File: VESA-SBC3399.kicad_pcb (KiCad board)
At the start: 2 copper layers, 54 parts, among them U1 RK3399

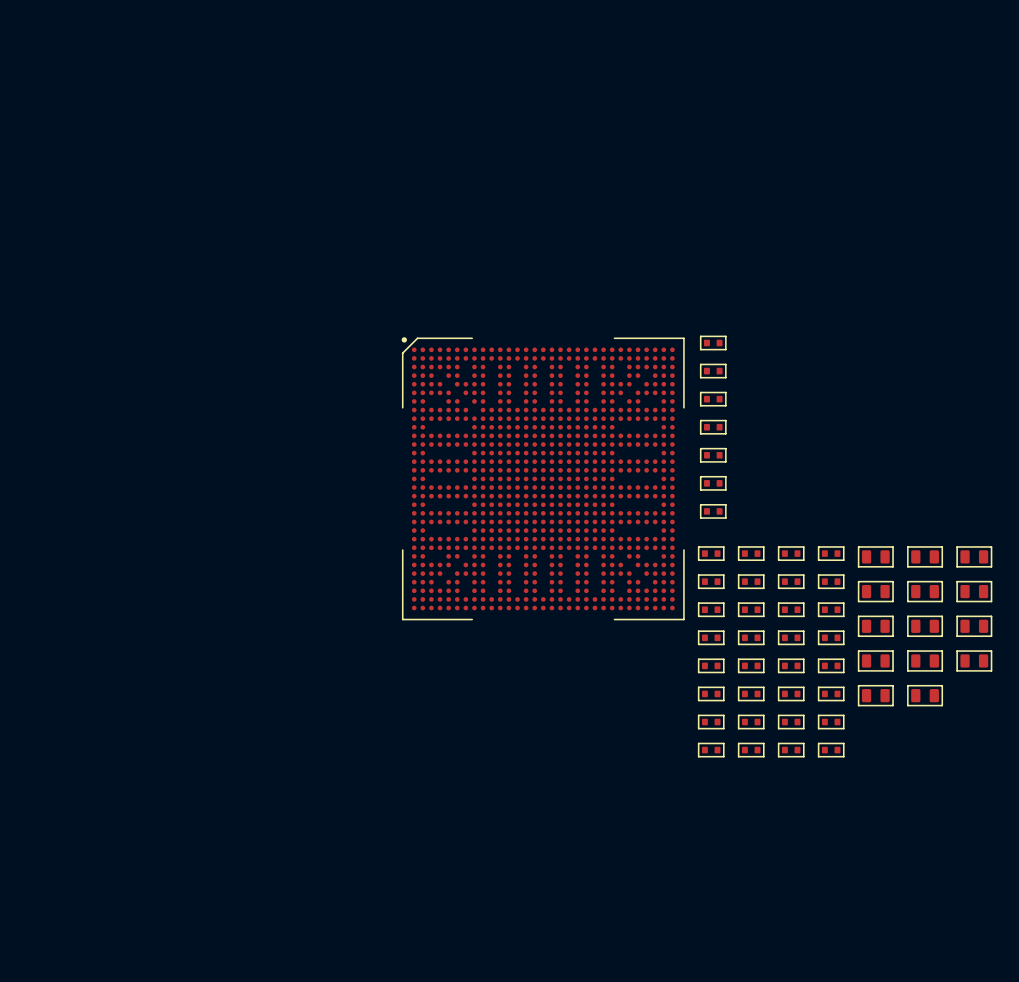
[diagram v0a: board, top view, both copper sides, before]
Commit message: design USB-A
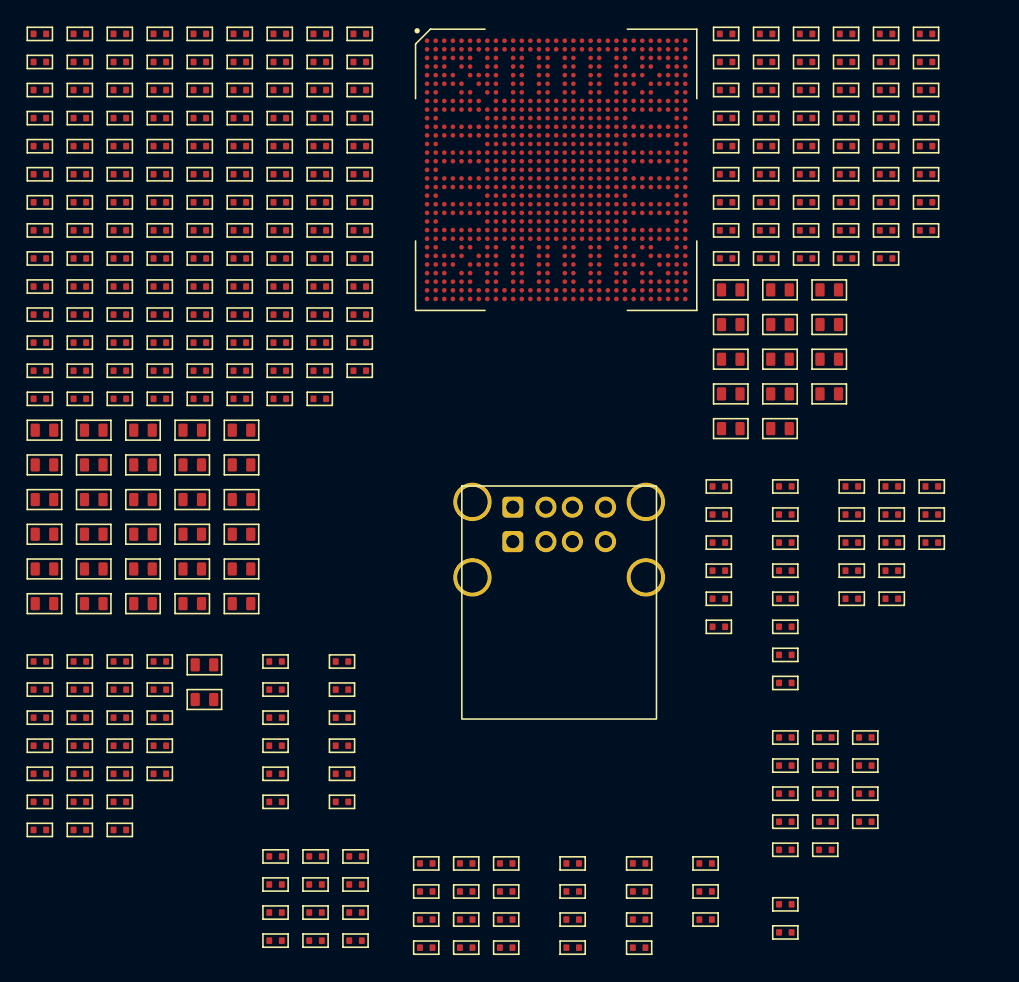
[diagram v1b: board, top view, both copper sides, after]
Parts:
- removed C1, C11, C12, C25, C26, C27, C48, C5, C6: ~, footprints:CAPC1005X50N
- removed C22, C3, C35, C36: ~, footprints:CAPC1608X80N
- removed U1: RK3399, footprints:BGA828C65P31X31_2100X2100X161
- added C100: ~, footprints:CAPC1005X50N, F.Cu at (125.8, 64.6)
- added C101: ~, footprints:CAPC1005X50N, F.Cu at (125.8, 66.8)
- added C102: ~, footprints:CAPC1005X50N, F.Cu at (125.8, 68.9)
- added C103: ~, footprints:CAPC1608X80N, F.Cu at (129.0, 97.2)
- added C104: ~, footprints:CAPC1005X50N, F.Cu at (125.8, 71.0)
- added C105: ~, footprints:CAPC1005X50N, F.Cu at (125.8, 73.1)
- added C106: ~, footprints:CAPC1005X50N, F.Cu at (125.8, 75.2)
- added C107: ~, footprints:CAPC1005X50N, F.Cu at (125.8, 77.4)
- added C108: ~, footprints:CAPC1005X50N, F.Cu at (125.8, 79.5)
- added C109: ~, footprints:CAPC1005X50N, F.Cu at (125.8, 81.6)
- added C110: ~, footprints:CAPC1005X50N, F.Cu at (125.8, 83.7)
- added C111: ~, footprints:CAPC1005X50N, F.Cu at (125.8, 85.8)
- added C112: ~, footprints:CAPC1608X80N, F.Cu at (129.0, 99.8)
- added C113: ~, footprints:CAPC1005X50N, F.Cu at (125.8, 88.0)
- added C114: ~, footprints:CAPC1005X50N, F.Cu at (125.8, 90.1)
- added C115: ~, footprints:CAPC1005X50N, F.Cu at (125.8, 92.2)
- added C116: ~, footprints:CAPC1005X50N, F.Cu at (128.8, 64.6)
- added C117: ~, footprints:CAPC1005X50N, F.Cu at (128.8, 66.8)
- added C118: ~, footprints:CAPC1005X50N, F.Cu at (128.8, 68.9)
- added C119: ~, footprints:CAPC1005X50N, F.Cu at (128.8, 71.0)
- added C120: ~, footprints:CAPC1608X80N, F.Cu at (129.0, 102.4)
- added C121: ~, footprints:CAPC1608X80N, F.Cu at (129.0, 105.0)
- added C122: ~, footprints:CAPC1005X50N, F.Cu at (128.8, 73.1)
- added C123: ~, footprints:CAPC1005X50N, F.Cu at (128.8, 75.2)
- added C124: ~, footprints:CAPC1005X50N, F.Cu at (128.8, 77.4)
- added C125: ~, footprints:CAPC1608X80N, F.Cu at (129.0, 107.7)
- added C126: ~, footprints:CAPC1005X50N, F.Cu at (128.8, 79.5)
- added C127: ~, footprints:CAPC1005X50N, F.Cu at (128.8, 81.6)
- added C128: ~, footprints:CAPC1005X50N, F.Cu at (128.8, 83.7)
- added C129: ~, footprints:CAPC1005X50N, F.Cu at (128.8, 85.8)
- added C130: ~, footprints:CAPC1005X50N, F.Cu at (128.8, 88.0)
- added C131: ~, footprints:CAPC1005X50N, F.Cu at (128.8, 90.1)
- added C132: ~, footprints:CAPC1005X50N, F.Cu at (165.6, 64.6)
- added C133: ~, footprints:CAPC1608X80N, F.Cu at (165.9, 84.0)
- added C134: ~, footprints:CAPC1608X80N, F.Cu at (165.9, 86.6)
- added C135: ~, footprints:CAPC1608X80N, F.Cu at (165.9, 89.2)
- added C136: ~, footprints:CAPC1005X50N, F.Cu at (165.6, 66.8)
- added C137: ~, footprints:CAPC1005X50N, F.Cu at (165.6, 68.9)
- added C138: ~, footprints:CAPC1005X50N, F.Cu at (165.6, 71.0)
- added C139: ~, footprints:CAPC1005X50N, F.Cu at (165.6, 73.1)
- added C140: ~, footprints:CAPC1005X50N, F.Cu at (165.6, 75.2)
- added C141: ~, footprints:CAPC1005X50N, F.Cu at (165.6, 77.4)
- added C142: ~, footprints:CAPC1005X50N, F.Cu at (165.6, 79.5)
- added C143: ~, footprints:CAPC1005X50N, F.Cu at (165.6, 81.6)
- added C144: ~, footprints:CAPC1608X80N, F.Cu at (165.9, 91.8)
- added C145: ~, footprints:CAPC1608X80N, F.Cu at (165.9, 94.5)
- added C146: ~, footprints:CAPC1005X50N, F.Cu at (168.6, 64.6)
- added C147: ~, footprints:CAPC1005X50N, F.Cu at (168.6, 66.8)
- added C148: ~, footprints:CAPC1005X50N, F.Cu at (168.6, 68.9)
- added C149: ~, footprints:CAPC1005X50N, F.Cu at (168.6, 71.0)
- added C150: ~, footprints:CAPC1005X50N, F.Cu at (168.6, 73.1)
- added C151: ~, footprints:CAPC1005X50N, F.Cu at (168.6, 75.2)
- added C152: ~, footprints:CAPC1005X50N, F.Cu at (168.6, 77.4)
- added C153: ~, footprints:CAPC1608X80N, F.Cu at (169.6, 84.0)
- added C154: ~, footprints:CAPC1608X80N, F.Cu at (169.6, 86.6)
- added C155: ~, footprints:CAPC1608X80N, F.Cu at (169.6, 89.2)
- added C156: ~, footprints:CAPC1005X50N, F.Cu at (168.6, 79.5)
- added C157: ~, footprints:CAPC1005X50N, F.Cu at (168.6, 81.6)
- added C158: ~, footprints:CAPC1005X50N, F.Cu at (171.6, 64.6)
- added C159: ~, footprints:CAPC1005X50N, F.Cu at (171.6, 66.8)
- added C160: ~, footprints:CAPC1005X50N, F.Cu at (171.6, 68.9)
- added C161: ~, footprints:CAPC1005X50N, F.Cu at (171.6, 71.0)
- added C162: ~, footprints:CAPC1005X50N, F.Cu at (171.6, 73.1)
- added C163: ~, footprints:CAPC1005X50N, F.Cu at (171.6, 75.2)
- added C164: ~, footprints:CAPC1608X80N, F.Cu at (169.6, 91.8)
- added C165: ~, footprints:CAPC1608X80N, F.Cu at (169.6, 94.5)
- added C166: ~, footprints:CAPC1608X80N, F.Cu at (173.3, 84.0)
- added C167: ~, footprints:CAPC1608X80N, F.Cu at (173.3, 86.6)
- added C168: ~, footprints:CAPC1005X50N, F.Cu at (171.6, 77.4)
- added C169: ~, footprints:CAPC1608X80N, F.Cu at (173.3, 89.2)
- added C170: ~, footprints:CAPC1005X50N, F.Cu at (171.6, 79.5)
- added C171: ~, footprints:CAPC1005X50N, F.Cu at (171.6, 81.6)
- added C172: ~, footprints:CAPC1005X50N, F.Cu at (174.6, 64.6)
- added C173: ~, footprints:CAPC1005X50N, F.Cu at (174.6, 66.8)
- added C174: ~, footprints:CAPC1005X50N, F.Cu at (174.6, 68.9)
- added C175: ~, footprints:CAPC1005X50N, F.Cu at (174.6, 71.0)
- added C176: ~, footprints:CAPC1005X50N, F.Cu at (174.6, 73.1)
- added C177: ~, footprints:CAPC1608X80N, F.Cu at (173.3, 91.8)
- added C178: ~, footprints:CAPC1005X50N, F.Cu at (174.6, 75.2)
- added C179: ~, footprints:CAPC1005X50N, F.Cu at (174.6, 77.4)
- added C180: ~, footprints:CAPC1005X50N, F.Cu at (174.6, 79.5)
- added C181: ~, footprints:CAPC1005X50N, F.Cu at (174.6, 81.6)
- added C182: ~, footprints:CAPC1005X50N, F.Cu at (177.6, 64.6)
- added C183: ~, footprints:CAPC1005X50N, F.Cu at (177.6, 66.8)
- added C184: ~, footprints:CAPC1005X50N, F.Cu at (177.6, 68.9)
- added C185: ~, footprints:CAPC1005X50N, F.Cu at (177.6, 71.0)
- added C186: ~, footprints:CAPC1005X50N, F.Cu at (177.6, 73.1)
- added C187: ~, footprints:CAPC1005X50N, F.Cu at (177.6, 75.2)
- added C188: ~, footprints:CAPC1005X50N, F.Cu at (177.6, 77.4)
- added C189: ~, footprints:CAPC1005X50N, F.Cu at (177.6, 79.5)
- added C190: ~, footprints:CAPC1005X50N, F.Cu at (177.6, 81.6)
- added C191: ~, footprints:CAPC1005X50N, F.Cu at (180.7, 64.6)
- added C192: ~, footprints:CAPC1005X50N, F.Cu at (180.7, 66.8)
- added C193: ~, footprints:CAPC1005X50N, F.Cu at (180.7, 68.9)
- added C194: ~, footprints:CAPC1005X50N, F.Cu at (180.7, 71.0)
- added C195: ~, footprints:CAPC1005X50N, F.Cu at (180.7, 73.1)
- added C196: ~, footprints:CAPC1005X50N, F.Cu at (180.7, 75.2)
- added C197: ~, footprints:CAPC1005X50N, F.Cu at (142.9, 127.3)
- added C198: ~, footprints:CAPC1005X50N, F.Cu at (142.9, 129.4)
- added C199: ~, footprints:CAPC1005X50N, F.Cu at (142.9, 131.5)
- added C200: ~, footprints:CAPC1005X50N, F.Cu at (142.9, 133.7)
- added C201: ~, footprints:CAPC1005X50N, F.Cu at (145.9, 127.3)
- added C202: ~, footprints:CAPC1005X50N, F.Cu at (159.0, 127.3)
- added C203: ~, footprints:CAPC1005X50N, F.Cu at (159.0, 129.4)
- added C204: ~, footprints:CAPC1005X50N, F.Cu at (170.0, 130.4)
- added C205: ~, footprints:CAPC1005X50N, F.Cu at (170.0, 132.5)
- added C206: ~, footprints:CAPC1005X50N, F.Cu at (170.0, 98.8)
- added C207: ~, footprints:CAPC1005X50N, F.Cu at (170.0, 100.9)
- added C208: ~, footprints:CAPC1608X80N, F.Cu at (126.2, 112.3)
- added C209: ~, footprints:CAPC1005X50N, F.Cu at (113.7, 112.0)
- added C210: ~, footprints:CAPC1005X50N, F.Cu at (113.7, 114.2)
- added C211: ~, footprints:CAPC1005X50N, F.Cu at (113.7, 116.3)
- added C212: ~, footprints:CAPC1005X50N, F.Cu at (113.7, 118.4)
- added C213: ~, footprints:CAPC1005X50N, F.Cu at (113.7, 120.5)
- added C214: ~, footprints:CAPC1005X50N, F.Cu at (113.7, 122.6)
- added C215: ~, footprints:CAPC1005X50N, F.Cu at (113.7, 124.8)
- added C216: ~, footprints:CAPC1005X50N, F.Cu at (116.7, 112.0)
- added C217: ~, footprints:CAPC1608X80N, F.Cu at (126.2, 114.9)
- added C218: ~, footprints:CAPC1005X50N, F.Cu at (116.7, 114.2)
- added C219: ~, footprints:CAPC1005X50N, F.Cu at (116.7, 116.3)
- added C220: ~, footprints:CAPC1005X50N, F.Cu at (116.7, 118.4)
- added C221: ~, footprints:CAPC1005X50N, F.Cu at (116.7, 120.5)
- added C222: ~, footprints:CAPC1005X50N, F.Cu at (116.7, 122.6)
- added C223: ~, footprints:CAPC1005X50N, F.Cu at (116.7, 124.8)
- added C224: ~, footprints:CAPC1005X50N, F.Cu at (119.8, 112.0)
- added C225: ~, footprints:CAPC1005X50N, F.Cu at (119.8, 114.2)
- added C226: ~, footprints:CAPC1005X50N, F.Cu at (119.8, 116.3)
- added C227: ~, footprints:CAPC1005X50N, F.Cu at (119.8, 118.4)
- added C228: ~, footprints:CAPC1005X50N, F.Cu at (119.8, 120.5)
- added C229: ~, footprints:CAPC1005X50N, F.Cu at (119.8, 122.6)
- added C230: ~, footprints:CAPC1005X50N, F.Cu at (119.8, 124.8)
- added C231: ~, footprints:CAPC1005X50N, F.Cu at (122.8, 112.0)
- added C232: ~, footprints:CAPC1005X50N, F.Cu at (175.0, 98.8)
- added C233: ~, footprints:CAPC1005X50N, F.Cu at (175.0, 100.9)
- added C234: ~, footprints:CAPC1005X50N, F.Cu at (175.0, 103.1)
- added C235: ~, footprints:CAPC1005X50N, F.Cu at (175.0, 105.2)
- added C236: ~, footprints:CAPC1005X50N, F.Cu at (175.0, 107.3)
- added C237: ~, footprints:CAPC1005X50N, F.Cu at (178.1, 98.8)
- added C238: ~, footprints:CAPC1005X50N, F.Cu at (178.1, 100.9)
- added C239: ~, footprints:CAPC1005X50N, F.Cu at (178.1, 103.1)
- added C240: ~, footprints:CAPC1005X50N, F.Cu at (178.1, 105.2)
- added C241: ~, footprints:CAPC1005X50N, F.Cu at (154.0, 127.3)
- added C242: ~, footprints:CAPC1005X50N, F.Cu at (154.0, 129.4)
- added C243: ~, footprints:CAPC1005X50N, F.Cu at (164.0, 127.3)
- added C244: ~, footprints:CAPC1005X50N, F.Cu at (170.0, 117.8)
- added C245: ~, footprints:CAPC1005X50N, F.Cu at (170.0, 119.9)
- added C246: ~, footprints:CAPC1005X50N, F.Cu at (170.0, 122.0)
- added C247: ~, footprints:CAPC1005X50N, F.Cu at (170.0, 124.1)
- added C248: ~, footprints:CAPC1005X50N, F.Cu at (131.5, 126.8)
- added C54: ~, footprints:CAPC1005X50N, F.Cu at (116.7, 92.2)
- added C56: ~, footprints:CAPC1005X50N, F.Cu at (119.8, 64.6)
- added C57: ~, footprints:CAPC1005X50N, F.Cu at (119.8, 66.8)
- added C58: ~, footprints:CAPC1005X50N, F.Cu at (119.8, 68.9)
- added C59: ~, footprints:CAPC1608X80N, F.Cu at (117.8, 107.7)
- added C60: ~, footprints:CAPC1608X80N, F.Cu at (121.5, 94.6)
- added C61: ~, footprints:CAPC1005X50N, F.Cu at (119.8, 71.0)
- added C62: ~, footprints:CAPC1005X50N, F.Cu at (119.8, 73.1)
- added C63: ~, footprints:CAPC1005X50N, F.Cu at (119.8, 75.2)
- added C64: ~, footprints:CAPC1608X80N, F.Cu at (121.5, 97.2)
- added C65: ~, footprints:CAPC1608X80N, F.Cu at (121.5, 99.8)
- added C66: ~, footprints:CAPC1608X80N, F.Cu at (121.5, 102.4)
- added C67: ~, footprints:CAPC1005X50N, F.Cu at (119.8, 77.4)
- added C68: ~, footprints:CAPC1005X50N, F.Cu at (119.8, 79.5)
- added C69: ~, footprints:CAPC1005X50N, F.Cu at (119.8, 81.6)
- added C70: ~, footprints:CAPC1608X80N, F.Cu at (121.5, 105.0)
- added C71: ~, footprints:CAPC1608X80N, F.Cu at (121.5, 107.7)
- added C72: ~, footprints:CAPC1005X50N, F.Cu at (119.8, 83.7)
- added C73: ~, footprints:CAPC1005X50N, F.Cu at (119.8, 85.8)
- added C74: ~, footprints:CAPC1608X80N, F.Cu at (125.2, 94.6)
- added C77: ~, footprints:CAPC1005X50N, F.Cu at (119.8, 88.0)
- added C78: ~, footprints:CAPC1005X50N, F.Cu at (119.8, 90.1)
- added C79: ~, footprints:CAPC1005X50N, F.Cu at (119.8, 92.2)
- added C80: ~, footprints:CAPC1005X50N, F.Cu at (122.8, 64.6)
- added C81: ~, footprints:CAPC1005X50N, F.Cu at (122.8, 66.8)
- added C82: ~, footprints:CAPC1005X50N, F.Cu at (122.8, 68.9)
- added C83: ~, footprints:CAPC1005X50N, F.Cu at (122.8, 71.0)
- added C84: ~, footprints:CAPC1005X50N, F.Cu at (122.8, 73.1)
- added C85: ~, footprints:CAPC1608X80N, F.Cu at (125.2, 97.2)
- added C86: ~, footprints:CAPC1608X80N, F.Cu at (125.2, 99.8)
- added C87: ~, footprints:CAPC1608X80N, F.Cu at (125.2, 102.4)
- added C88: ~, footprints:CAPC1005X50N, F.Cu at (122.8, 75.2)
- added C89: ~, footprints:CAPC1005X50N, F.Cu at (122.8, 77.4)
- added C90: ~, footprints:CAPC1005X50N, F.Cu at (122.8, 79.5)
- added C91: ~, footprints:CAPC1005X50N, F.Cu at (122.8, 81.6)
- added C92: ~, footprints:CAPC1005X50N, F.Cu at (122.8, 83.7)
- added C93: ~, footprints:CAPC1608X80N, F.Cu at (125.2, 105.0)
- added C94: ~, footprints:CAPC1005X50N, F.Cu at (122.8, 85.8)
- added C95: ~, footprints:CAPC1005X50N, F.Cu at (122.8, 88.0)
- added C96: ~, footprints:CAPC1608X80N, F.Cu at (125.2, 107.7)
- added C97: ~, footprints:CAPC1608X80N, F.Cu at (129.0, 94.6)
- added C98: ~, footprints:CAPC1005X50N, F.Cu at (122.8, 90.1)
- added C99: ~, footprints:CAPC1005X50N, F.Cu at (122.8, 92.2)
- added CON1: AF SS-JB17.6, footprints:AF SS-JB17.6, F.Cu at (152.9, 101.7)
- added R1: ~, footprints:RESC1005X35N, F.Cu at (165.0, 103.1)
- added R100: ~, footprints:RESC1005X35N, F.Cu at (173.0, 122.0)
- added R101: ~, footprints:RESC1005X35N, F.Cu at (173.0, 124.1)
- added R102: ~, footprints:RESC1005X35N, F.Cu at (173.0, 126.3)
- added R103: ~, footprints:RESC1005X35N, F.Cu at (176.1, 117.8)
- added R104: ~, footprints:RESC1005X35N, F.Cu at (176.1, 119.9)
- added R105: ~, footprints:RESC1005X35N, F.Cu at (176.1, 122.0)
- added R106: ~, footprints:RESC1005X35N, F.Cu at (176.1, 124.1)
- added R107: ~, footprints:RESC1005X35N, F.Cu at (131.5, 128.9)
- added R108: ~, footprints:RESC1005X35N, F.Cu at (131.5, 131.0)
- added R109: ~, footprints:RESC1005X35N, F.Cu at (131.5, 133.1)
- added R11: ~, footprints:RESC1005X35N, F.Cu at (131.8, 66.8)
- added R110: ~, footprints:RESC1005X35N, F.Cu at (134.5, 126.8)
- added R111: ~, footprints:RESC1005X35N, F.Cu at (134.5, 128.9)
- added R112: ~, footprints:RESC1005X35N, F.Cu at (134.5, 131.0)
- added R113: ~, footprints:RESC1005X35N, F.Cu at (134.5, 133.1)
- added R114: ~, footprints:RESC1005X35N, F.Cu at (137.6, 126.8)
- added R115: ~, footprints:RESC1005X35N, F.Cu at (137.6, 128.9)
- added R116: ~, footprints:RESC1005X35N, F.Cu at (137.6, 131.0)
- added R117: ~, footprints:RESC1005X35N, F.Cu at (137.6, 133.1)
- added R118: ~, footprints:RESC1005X35N, F.Cu at (131.5, 112.0)
- added R119: ~, footprints:RESC1005X35N, F.Cu at (131.5, 114.2)
- added R12: ~, footprints:RESC1005X35N, F.Cu at (131.8, 68.9)
- added R120: ~, footprints:RESC1005X35N, F.Cu at (131.5, 116.3)
- added R121: ~, footprints:RESC1005X35N, F.Cu at (131.5, 118.4)
- added R122: ~, footprints:RESC1005X35N, F.Cu at (131.5, 120.5)
- added R123: ~, footprints:RESC1005X35N, F.Cu at (131.5, 122.6)
- added R13: ~, footprints:RESC1005X35N, F.Cu at (131.8, 71.0)
- added R14: ~, footprints:RESC1005X35N, F.Cu at (131.8, 73.1)
- added R15: ~, footprints:RESC1005X35N, F.Cu at (131.8, 75.2)
- added R17: ~, footprints:RESC1005X35N, F.Cu at (131.8, 77.4)
- added R18: ~, footprints:RESC1005X35N, F.Cu at (131.8, 79.5)
- added R2: ~, footprints:RESC1005X35N, F.Cu at (165.0, 105.2)
- added R21: ~, footprints:RESC1005X35N, F.Cu at (131.8, 81.6)
- added R22: ~, footprints:RESC1005X35N, F.Cu at (131.8, 83.7)
- added R23: ~, footprints:RESC1005X35N, F.Cu at (131.8, 85.8)
- added R24: ~, footprints:RESC1005X35N, F.Cu at (131.8, 88.0)
- added R25: ~, footprints:RESC1005X35N, F.Cu at (131.8, 90.1)
- added R26: ~, footprints:RESC1005X35N, F.Cu at (131.8, 92.2)
- added R27: ~, footprints:RESC1005X35N, F.Cu at (134.9, 64.6)
- added R28: ~, footprints:RESC1005X35N, F.Cu at (134.9, 66.8)
- added R29: ~, footprints:RESC1005X35N, F.Cu at (134.9, 68.9)
- added R30: ~, footprints:RESC1005X35N, F.Cu at (134.9, 71.0)
- added R31: ~, footprints:RESC1005X35N, F.Cu at (134.9, 73.1)
- added R32: ~, footprints:RESC1005X35N, F.Cu at (134.9, 75.2)
- added R33: ~, footprints:RESC1005X35N, F.Cu at (134.9, 77.4)
- added R34: ~, footprints:RESC1005X35N, F.Cu at (134.9, 79.5)
- added R35: ~, footprints:RESC1005X35N, F.Cu at (134.9, 81.6)
- added R36: ~, footprints:RESC1005X35N, F.Cu at (134.9, 83.7)
- added R37: ~, footprints:RESC1005X35N, F.Cu at (134.9, 85.8)
- added R39: ~, footprints:RESC1005X35N, F.Cu at (134.9, 88.0)
- added R4: ~, footprints:RESC1005X35N, F.Cu at (165.0, 107.3)
- added R40: ~, footprints:RESC1005X35N, F.Cu at (134.9, 90.1)
- added R41: ~, footprints:RESC1005X35N, F.Cu at (134.9, 92.2)
- added R43: ~, footprints:RESC1005X35N, F.Cu at (137.9, 64.6)
- added R44: ~, footprints:RESC1005X35N, F.Cu at (137.9, 66.8)
- added R45: ~, footprints:RESC1005X35N, F.Cu at (137.9, 68.9)
- added R46: ~, footprints:RESC1005X35N, F.Cu at (137.9, 71.0)
- added R47: ~, footprints:RESC1005X35N, F.Cu at (137.9, 73.1)
- added R48: ~, footprints:RESC1005X35N, F.Cu at (137.9, 75.2)
- added R5: ~, footprints:RESC1005X35N, F.Cu at (165.0, 109.4)
- added R50: ~, footprints:RESC1005X35N, F.Cu at (137.9, 77.4)
- added R51: ~, footprints:RESC1005X35N, F.Cu at (137.9, 79.5)
- added R52: ~, footprints:RESC1005X35N, F.Cu at (137.9, 81.6)
- added R53: ~, footprints:RESC1005X35N, F.Cu at (137.9, 83.7)
- added R55: ~, footprints:RESC1005X35N, F.Cu at (137.9, 85.8)
- added R56: ~, footprints:RESC1005X35N, F.Cu at (137.9, 88.0)
- added R57: ~, footprints:RESC1005X35N, F.Cu at (137.9, 90.1)
- added R60: ~, footprints:RESC1005X35N, F.Cu at (180.7, 77.4)
- added R61: ~, footprints:RESC1005X35N, F.Cu at (180.7, 79.5)
- added R62: ~, footprints:RESC1005X35N, F.Cu at (145.9, 129.4)
- added R63: ~, footprints:RESC1005X35N, F.Cu at (145.9, 131.5)
- added R64: ~, footprints:RESC1005X35N, F.Cu at (145.9, 133.7)
- added R65: ~, footprints:RESC1005X35N, F.Cu at (148.9, 127.3)
- added R66: ~, footprints:RESC1005X35N, F.Cu at (148.9, 129.4)
- added R67: ~, footprints:RESC1005X35N, F.Cu at (148.9, 131.5)
- added R68: ~, footprints:RESC1005X35N, F.Cu at (148.9, 133.7)
- added R69: ~, footprints:RESC1005X35N, F.Cu at (136.5, 112.0)
- added R7: ~, footprints:RESC1005X35N, F.Cu at (128.8, 92.2)
- added R70: ~, footprints:RESC1005X35N, F.Cu at (136.5, 114.2)
- added R71: ~, footprints:RESC1005X35N, F.Cu at (136.5, 116.3)
- added R72: ~, footprints:RESC1005X35N, F.Cu at (136.5, 118.4)
- added R73: ~, footprints:RESC1005X35N, F.Cu at (136.5, 120.5)
- added R74: ~, footprints:RESC1005X35N, F.Cu at (136.5, 122.6)
- added R75: ~, footprints:RESC1005X35N, F.Cu at (159.0, 131.5)
- added R76: ~, footprints:RESC1005X35N, F.Cu at (159.0, 133.7)
- added R77: ~, footprints:RESC1005X35N, F.Cu at (170.0, 103.1)
- added R78: ~, footprints:RESC1005X35N, F.Cu at (170.0, 105.2)
- added R79: ~, footprints:RESC1005X35N, F.Cu at (170.0, 107.3)
- added R80: ~, footprints:RESC1005X35N, F.Cu at (170.0, 109.4)
- added R81: ~, footprints:RESC1005X35N, F.Cu at (170.0, 111.5)
- added R82: ~, footprints:RESC1005X35N, F.Cu at (170.0, 113.7)
- added R83: ~, footprints:RESC1005X35N, F.Cu at (122.8, 114.2)
- added R84: ~, footprints:RESC1005X35N, F.Cu at (122.8, 116.3)
- added R85: ~, footprints:RESC1005X35N, F.Cu at (122.8, 118.4)
- added R86: ~, footprints:RESC1005X35N, F.Cu at (122.8, 120.5)
- added R87: ~, footprints:RESC1005X35N, F.Cu at (178.1, 107.3)
- added R88: ~, footprints:RESC1005X35N, F.Cu at (181.1, 98.8)
- added R89: ~, footprints:RESC1005X35N, F.Cu at (181.1, 100.9)
- added R9: ~, footprints:RESC1005X35N, F.Cu at (131.8, 64.6)
- added R90: ~, footprints:RESC1005X35N, F.Cu at (181.1, 103.1)
- added R93: ~, footprints:RESC1005X35N, F.Cu at (154.0, 131.5)
- added R94: ~, footprints:RESC1005X35N, F.Cu at (154.0, 133.7)
- added R95: ~, footprints:RESC1005X35N, F.Cu at (164.0, 129.4)
- added R96: ~, footprints:RESC1005X35N, F.Cu at (164.0, 131.5)
- added R97: ~, footprints:RESC1005X35N, F.Cu at (170.0, 126.3)
- added R98: ~, footprints:RESC1005X35N, F.Cu at (173.0, 117.8)
- added R99: ~, footprints:RESC1005X35N, F.Cu at (173.0, 119.9)
- added U11: RK3399, footprints:BGA828C65P31X31_2100X2100X161, F.Cu at (152.7, 74.9)
- C14, C2, C23, C24, C33, C34, C38, C4: footprint footprints:CAPC1608X80N -> footprints:CAPC1005X50N
- C17, C18, C19, C20, C39, C43, C44, C45, C49: footprint footprints:CAPC1005X50N -> footprints:CAPC1608X80N
- moved C34 78.5 mm to (116.7, 68.9)
- moved C33 78.2 mm to (116.7, 66.8)
- moved C38 76.7 mm to (116.7, 73.1)
- moved C14 75.6 mm to (113.7, 73.1)
- moved C24 71.6 mm to (113.7, 83.7)
- moved C23 71.4 mm to (113.7, 81.6)
- moved C46 67.2 mm to (117.8, 102.4)
- moved C32 66.5 mm to (116.7, 64.6)
- moved C13 65.2 mm to (114.1, 94.6)
- moved C37 64.1 mm to (116.7, 71.0)
- moved C40 64.1 mm to (116.7, 75.2)
- moved C41 64.1 mm to (116.7, 77.4)
- moved C42 64.1 mm to (116.7, 79.5)
- moved C50 63.6 mm to (116.7, 83.7)
- moved C52 63.6 mm to (116.7, 88.0)
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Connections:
- C10 pad 1: +0V9_VDD_CPU_B -> +12V_SYS
- C13 pad 1: +0V9_VDD_CPU_L -> +5V0_SYS
- C14 pad 1: +0V9_VDD_CPU_L -> +5V0_SYS
- C15 pad 1: +0V9_VDD_CPU_L -> +0V9_VDD_CPU_B
- C16 pad 1: +0V9_VDD_CPU_L -> +0V9_VDD_CPU_B
- C17 pad 1: +0V9_VDD_CPU_L -> +0V9_VDD_CPU_B
- C18 pad 1: +0V9_VDD_CPU_L -> +0V9_VDD_CPU_B
- C19 pad 1: +0V9_VDD_CPU_L -> +0V9_VDD_CPU_B
- C2 pad 1: +0V9_VDD_CPU_B -> +5V0_VBUS_USBA0
- C20 pad 1: +0V9_VDD_CPU_L -> +0V9_VDD_CPU_B
- C21 pad 1: +0V9_VDD_GPU -> /Power/12V_SYS_dVdT
- C23 pad 1: +0V9_VDD_GPU -> /Power/0V9_VDD_CPU_B_PWR_EN
- C24 pad 1: +0V9_VDD_GPU -> Net-(U3-BOOT)
- C24 pad 2: GND -> /Power/5V0_USB_SW
- C28 pad 1: +0V9_VDD_GPU -> +12V_SYS
- C29 pad 1: +0V9_VDD_GPU -> +12V_SYS
- C30 pad 1: +0V9_VDD_GPU -> +12V_SYS
- C31 pad 1: +0V9_VDD_GPU -> +12V_SYS
- C32 pad 1: +0V9_VDD_GPU -> +5V0_USB
- C33 pad 1: +0V9_VDD_GPU -> +5V0_USB
- C34 pad 1: +0V9_VDD_GPU -> +5V0_USB
- C37 pad 1: +0V9_VDD_CENTER -> /Power/5V0_USB_SS
- C38 pad 1: +0V9_VDD_CENTER -> Net-(U3-VCC)
- C39 pad 1: +0V9_VDD_CENTER -> +5V0_SYS
- C4 pad 1: +0V9_VDD_CPU_B -> +5V0_VBUS_USBA1
- C40 pad 1: +0V9_VDD_CENTER -> +5V0_SYS
- C41 pad 1: +0V9_VDD_CENTER -> +0V9_VDD_GPU
- C42 pad 1: +0V9_VDD_CENTER -> +0V9_VDD_GPU
- C43 pad 1: +0V9_VDD_CENTER -> +0V9_VDD_GPU
- C44 pad 1: +0V9_VDD_CENTER -> +0V9_VDD_GPU
- C45 pad 1: +0V9_VDD_LOG -> +0V9_VDD_GPU
- C46 pad 1: +0V9_VDD_LOG -> +0V9_VDD_GPU
- C47 pad 1: +0V9_VDD_LOG -> Net-(U5-VBST)
- C47 pad 2: GND -> /Power/5V0_SYS_SW
- C49 pad 1: +0V9_VDD_LOG -> +12V_SYS
- C50 pad 1: +0V9_VDD_LOG -> +12V_SYS
- C51 pad 1: +0V9_VDD_LOG -> /Power/0V9_VDD_GPU_PWR_EN
- C52 pad 1: +0V9_VDD_LOG -> +5V0_SYS
- C53 pad 1: +0V9_VDD_LOG -> +5V0_SYS
- C7 pad 1: +0V9_VDD_CPU_B -> +12V_DC_IN
- C8 pad 1: +0V9_VDD_CPU_B -> +12V_SYS
- C9 pad 1: +0V9_VDD_CPU_B -> +12V_SYS
